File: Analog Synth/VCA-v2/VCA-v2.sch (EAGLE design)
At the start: 43 parts, among them IC2 TL084D, Q1_ DMMT3904W, T3 2N3904

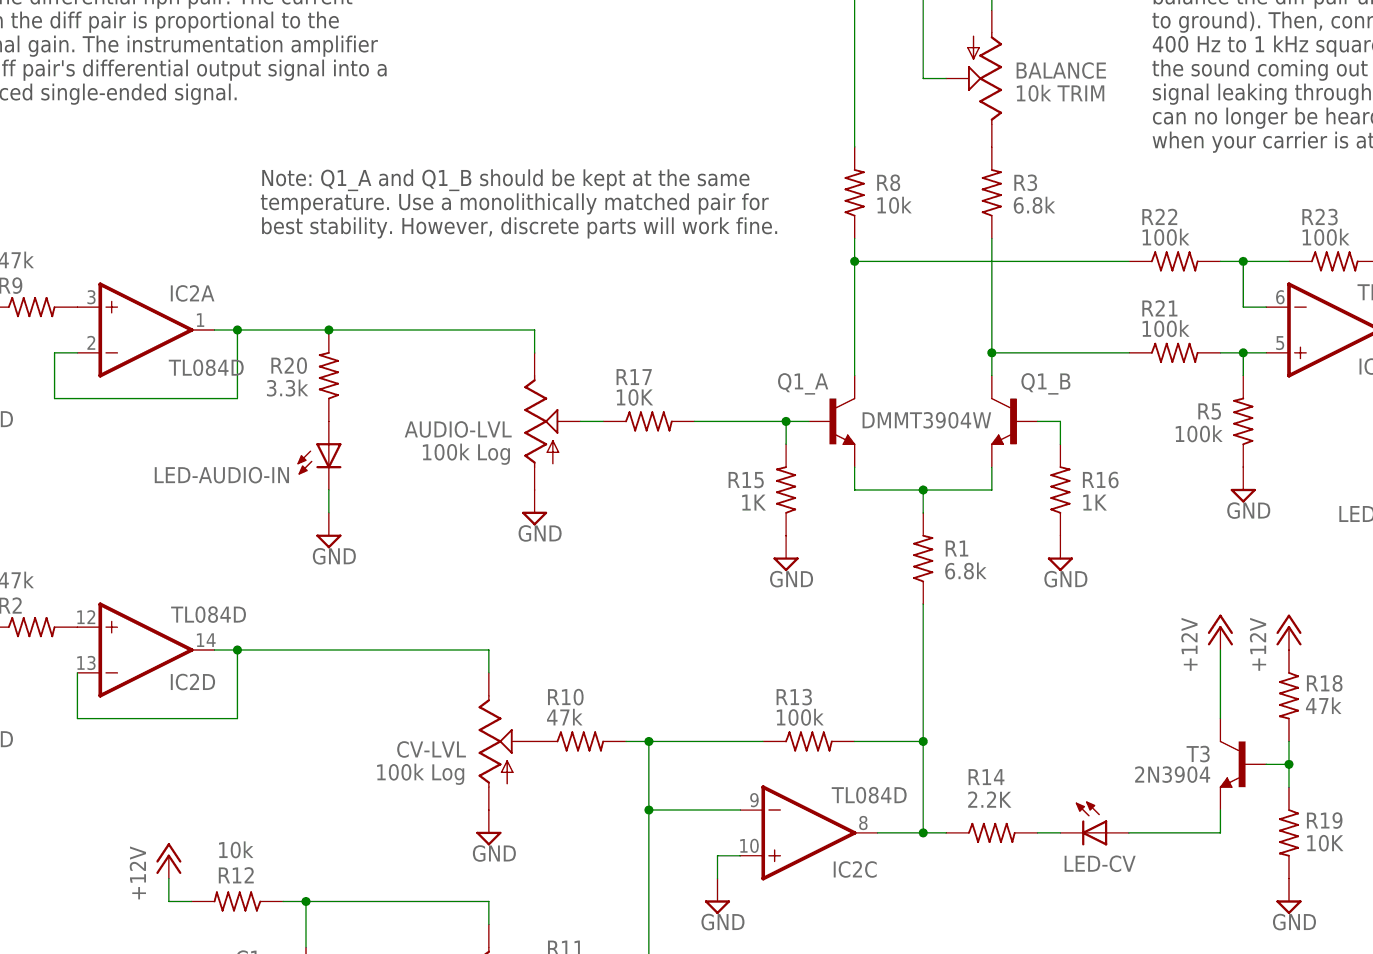
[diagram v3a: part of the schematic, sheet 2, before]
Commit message: making progress on VCA-v2. Updated the Eurorack power connector
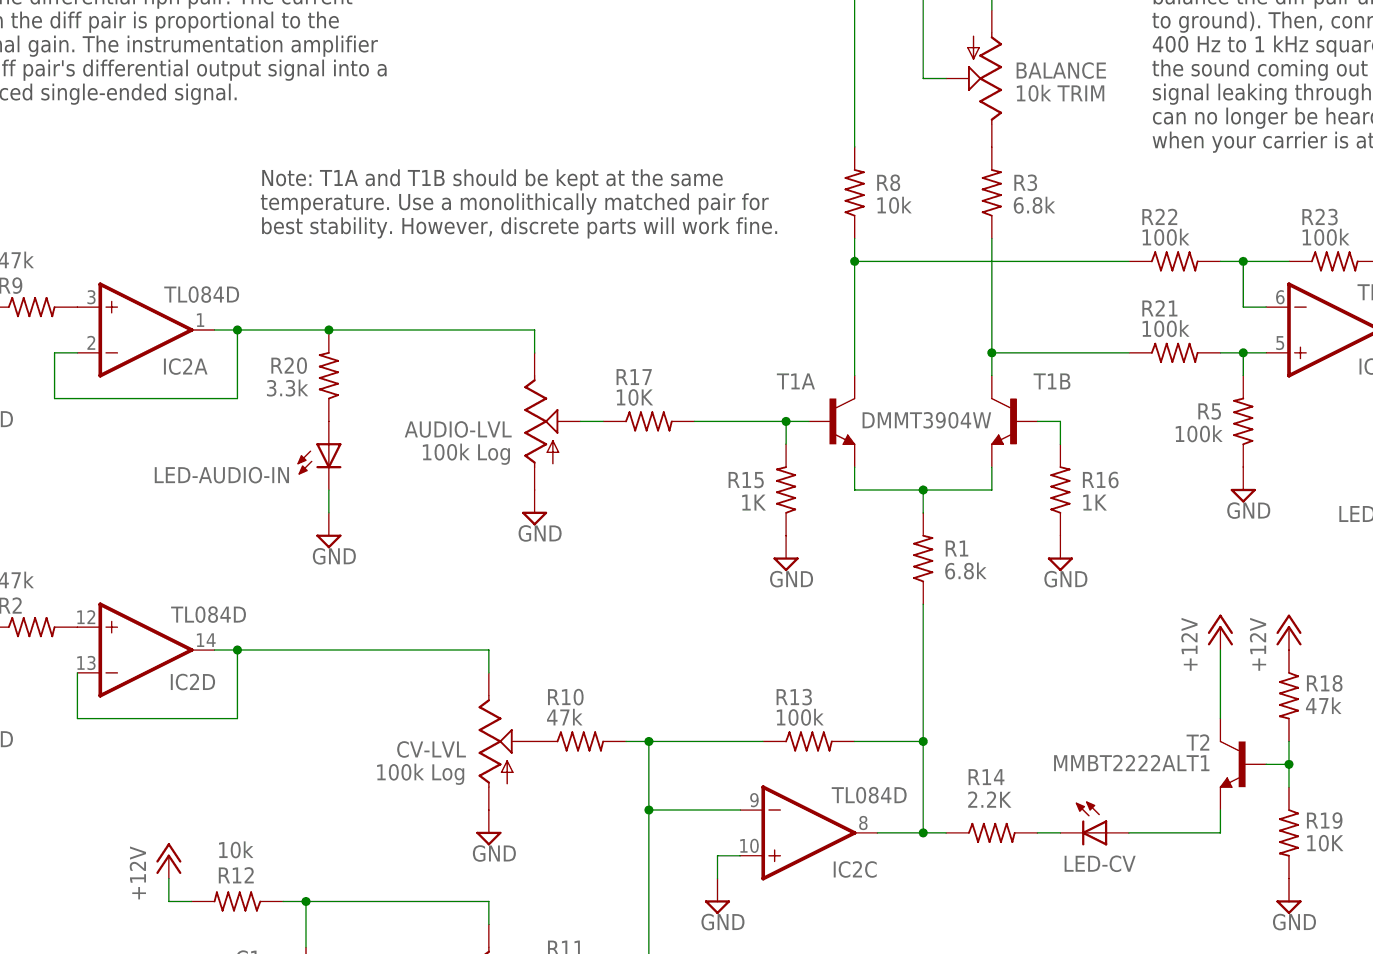
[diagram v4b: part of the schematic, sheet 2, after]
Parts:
- removed T3: 2N3904, transistor-neu-to92:2N3904
- added T2: MMBT2222ALT1, transistor:MMBT2222ALT1-NPN-SOT23-BEC
- renumbered Q1_ to T1
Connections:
- net +12V: now also T2.C; no longer T3.C
- net LED_SUPPLY: now also T2.E; no longer T3.E
- net N$20: now also T2.B; no longer T3.B
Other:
- note added: "Note: T1A and T1B should be kept at the same temperature. Use a monolithically matched pair for best stability. However, discrete parts will work fine."
- note removed: "Note: Q1_A and Q1_B should be kept at the same temperature. Use a monolithically matched pair for best stability. However, discrete parts will work fine."
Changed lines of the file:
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@@
 <part name="SUPPLY11" library="supply2" deviceset="GND" device=""/>
 <part name="R17" library="resistor" deviceset="R-US_" device="R0603" value="10K"/>
-<part name="T3" library="transistor-neu-to92" deviceset="2N3904" device=""/>
 <part name="P+5" library="supply1" deviceset="+12V" device=""/>
 <part name="R18" library="resistor" deviceset="R-US_" device="R0603" value="47k"/>
@@
 <part name="R24" library="resistor" deviceset="R-US_" device="R0603" value="3.3k"/>
 <part name="SUPPLY17" library="supply2" deviceset="GND" device=""/>
-<part name="Q1_" library="!synth_sch" deviceset="DMMT3904W" device=""/>
+<part name="T1" library="!synth_sch" deviceset="DMMT3904W" device=""/>
+<part name="T2" library="transistor" deviceset="*-NPN-" device="SOT23-BEC" technology="MMBT2222ALT1" value="MMBT2222ALT1"/>
 </parts>
 <sheets>
@@
 can no longer be heard at the output (tune for minimum volume). This ensures that
 when your carrier is at 0 V, your modulation signal has no effect on the output audio.</text>
-<text x="38.1" y="121.92" size="1.778" layer="97" rot="MR180">Note: Q1_A and Q1_B should be kept at the same
+<text x="38.1" y="121.92" size="1.778" layer="97" rot="MR180">Note: T1A and T1B should be kept at the same
 temperature. Use a monolithically matched pair for
 best stability. However, discrete parts will work fine.</text>
@@
 </instance>
 <instance part="IC2" gate="C" x="99.06" y="48.26" rot="MR180"/>
-<instance part="IC2" gate="A" x="25.4" y="104.14"/>
+<instance part="IC2" gate="A" x="25.4" y="104.14" smashed="yes">
+<attribute name="NAME" x="27.178" y="99.187" size="1.778" layer="95"/>
+<attribute name="VALUE" x="27.432" y="107.188" size="1.778" layer="96"/>
+</instance>
 <instance part="IC2" gate="B" x="157.48" y="104.14" rot="MR180"/>
 <instance part="CV-IN" gate="J1" x="-2.54" y="68.58" smashed="yes">
@@
 <attribute name="VALUE" x="77.47" y="95.758" size="1.778" layer="96"/>
 </instance>
-<instance part="T3" gate="G1" x="147.32" y="55.88" smashed="yes" rot="MR0">
-<attribute name="NAME" x="143.764" y="57.912" size="1.778" layer="95" rot="R180"/>
-<attribute name="VALUE" x="143.764" y="55.626" size="1.778" layer="96" rot="R180"/>
-</instance>
 <instance part="P+5" gate="1" x="144.78" y="71.12"/>
 <instance part="R18" gate="G$1" x="152.4" y="63.5" smashed="yes" rot="R270">
@@
 </instance>
 <instance part="SUPPLY17" gate="GND" x="177.8" y="81.28"/>
-<instance part="Q1_" gate="A" x="101.6" y="93.98" smashed="yes">
+<instance part="T1" gate="A" x="101.6" y="93.98" smashed="yes">
 <attribute name="NAME" x="95.504" y="97.536" size="1.778" layer="95"/>
 </instance>
-<instance part="Q1_" gate="B" x="121.92" y="93.98" smashed="yes" rot="MR0">
+<instance part="T1" gate="B" x="121.92" y="93.98" smashed="yes" rot="MR0">
 <attribute name="NAME" x="128.27" y="97.536" size="1.778" layer="95" rot="MR0"/>
 <attribute name="VALUE" x="119.38" y="93.218" size="1.778" layer="96" rot="MR0"/>
+</instance>
+<instance part="T2" gate="G$1" x="147.32" y="55.88" smashed="yes" rot="MR0">
+<attribute name="NAME" x="143.764" y="57.404" size="1.778" layer="95" rot="MR0"/>
+<attribute name="VALUE" x="143.764" y="55.118" size="1.778" layer="96" rot="MR0"/>
 </instance>
 </instances>
@@
 <junction x="104.14" y="111.76"/>
 <pinref part="R8" gate="G$1" pin="1"/>
-<pinref part="Q1_" gate="A" pin="C"/>
+<pinref part="T1" gate="A" pin="C"/>
 </segment>
 </net>
@@
 <junction x="119.38" y="101.6"/>
 <pinref part="R3" gate="G$1" pin="1"/>
-<pinref part="Q1_" gate="B" pin="C"/>
+<pinref part="T1" gate="B" pin="C"/>
 </segment>
 </net>
@@
 </segment>
 <segment>
-<pinref part="T3" gate="G1" pin="C"/>
 <wire x1="144.78" y1="60.96" x2="144.78" y2="68.58" width="0.1524" layer="91"/>
 <pinref part="P+5" gate="1" pin="+12V"/>
+<pinref part="T2" gate="G$1" pin="C"/>
 </segment>
 <segment>
@@
 <net name="LED_SUPPLY" class="0">
 <segment>
-<pinref part="T3" gate="G1" pin="E"/>
 <wire x1="144.78" y1="48.26" x2="144.78" y2="50.8" width="0.1524" layer="91"/>
 <pinref part="LED-CV" gate="G$1" pin="A"/>
 <wire x1="144.78" y1="48.26" x2="134.62" y2="48.26" width="0.1524" layer="91"/>
+<pinref part="T2" gate="G$1" pin="E"/>
 </segment>
 </net>
@@
 <wire x1="111.76" y1="83.82" x2="111.76" y2="86.36" width="0.1524" layer="91"/>
 <junction x="111.76" y="86.36"/>
-<pinref part="Q1_" gate="A" pin="E"/>
-<pinref part="Q1_" gate="B" pin="E"/>
+<pinref part="T1" gate="A" pin="E"/>
+<pinref part="T1" gate="B" pin="E"/>
 </segment>
 </net>
@@
 <wire x1="96.52" y1="91.44" x2="96.52" y2="93.98" width="0.1524" layer="91"/>
 <junction x="96.52" y="93.98"/>
-<pinref part="Q1_" gate="A" pin="B"/>
+<pinref part="T1" gate="A" pin="B"/>
 </segment>
 </net>
@@
 <pinref part="R16" gate="G$1" pin="2"/>
 <wire x1="127" y1="93.98" x2="127" y2="91.44" width="0.1524" layer="91"/>
-<pinref part="Q1_" gate="B" pin="B"/>
+<pinref part="T1" gate="B" pin="B"/>
 </segment>
 </net>
@@
 <pinref part="R19" gate="G$1" pin="1"/>
 <wire x1="152.4" y1="53.34" x2="152.4" y2="55.88" width="0.1524" layer="91"/>
-<pinref part="T3" gate="G1" pin="B"/>
 <wire x1="149.86" y1="55.88" x2="152.4" y2="55.88" width="0.1524" layer="91"/>
 <pinref part="R18" gate="G$1" pin="2"/>
 <wire x1="152.4" y1="55.88" x2="152.4" y2="58.42" width="0.1524" layer="91"/>
 <junction x="152.4" y="55.88"/>
-</segment>
-</net>
+<pinref part="T2" gate="G$1" pin="B"/>
+</segment>
+</net>

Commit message: making some progress on VCA-v2
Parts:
- C6, C7: device capacitor-wima:C2.5/2 -> rcl:C-EUC0603
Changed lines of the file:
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@@
 <part name="P-2" library="supply1" deviceset="-12V" device=""/>
 <part name="SUPPLY9" library="supply2" deviceset="GND" device=""/>
-<part name="C6" library="capacitor-wima" deviceset="C" device="2.5/2" value="0.01µ"/>
-<part name="C7" library="capacitor-wima" deviceset="C" device="2.5/2" value="0.01µ"/>
+<part name="C6" library="rcl" deviceset="C-EU" device="C0603" value="0.01µ"/>
+<part name="C7" library="rcl" deviceset="C-EU" device="C0603" value="0.01µ"/>
 <part name="CV-IN" library="!synth_sch" deviceset="MONO_JACK" device="" value="I/O"/>
 <part name="AUDIO-IN" library="!synth_sch" deviceset="MONO_JACK" device="" value="I/O"/>
